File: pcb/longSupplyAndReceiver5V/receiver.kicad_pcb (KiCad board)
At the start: 2 copper layers, 20 x 16 mm, 7 parts, among them J1 WAGO 2061-602, J2 har-flexicon 2,54 MSH-4, J3 Conn_01x05_Socket, J4 Kyocera-009176002001906, U1 SP485CN

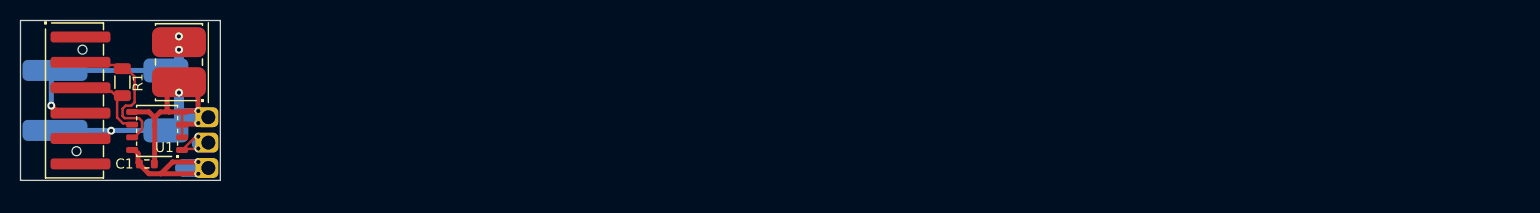
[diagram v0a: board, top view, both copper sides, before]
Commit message: New pin ordering for Harting connector
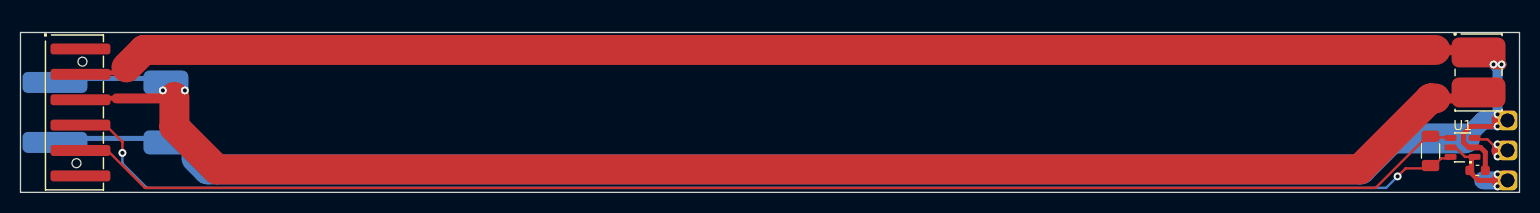
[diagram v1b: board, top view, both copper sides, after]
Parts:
- C1: footprint local:0603 -> Capacitor_SMD:C_0603_1608Metric
- J3: footprint local:HolesL -> local:SolderHoles3pin10mm
- R1: footprint local:1206 -> Resistor_SMD:R_1206_3216Metric
- U1: value SP485CN -> ISL3281E; footprint local:SO-8 -> local:ISL3281E
- moved C1 133.2 mm to (245.8, 107.0)
- moved R1 131.1 mm to (241.1, 105.0)
- moved U1 130.6 mm to (244.3, 104.7)
- moved J4 130.0 mm to (245.9, 97.2), turned to -90 degrees
- moved J3 130.0 mm to (248.8, 105.0)
- moved J2 1.20 mm to (106.0, 101.2)
- moved J1 1.20 mm to (108.2, 101.2)
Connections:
- J2 pad 1: RS485_B -> GND
- J2 pad 2: RS485_A -> +15V
- J2 pad 3: +15V -> RS485_A
- J2 pad 4: GND -> RS485_B
- U1 pad 1: DATA -> +5V
- U1 pad 3: GND -> DATA
- U1 pad 4: GND -> RS485_B
- U1 pad 5: GND -> +5V
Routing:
- net GND: track 40.2 -> 308.5 mm
- net +15V: track 20.2 -> 159.9 mm, vias 3 -> 2
- net RS485_A: track 8.21 -> 142.3 mm, vias 0 -> 2
- net RS485_B: track 19.4 -> 140.9 mm
- net +5V: track 19.0 -> 13.4 mm
- net DATA: track 8.68 -> 9.59 mm
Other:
- board size 20 x 16 mm -> 150 x 16 mm
- board text added: "LED Strip"
